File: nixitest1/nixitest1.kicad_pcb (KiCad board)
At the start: 2 copper layers, 22 x 38.2 mm, 34 parts, among them J1 MSYS, Q1 60V 3A, Q10 HVN, Q11 HVN, Q12 HVN, Q13 HVN, Q2 HVN, Q3 HVN, Q4 HVN, Q5 HVN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

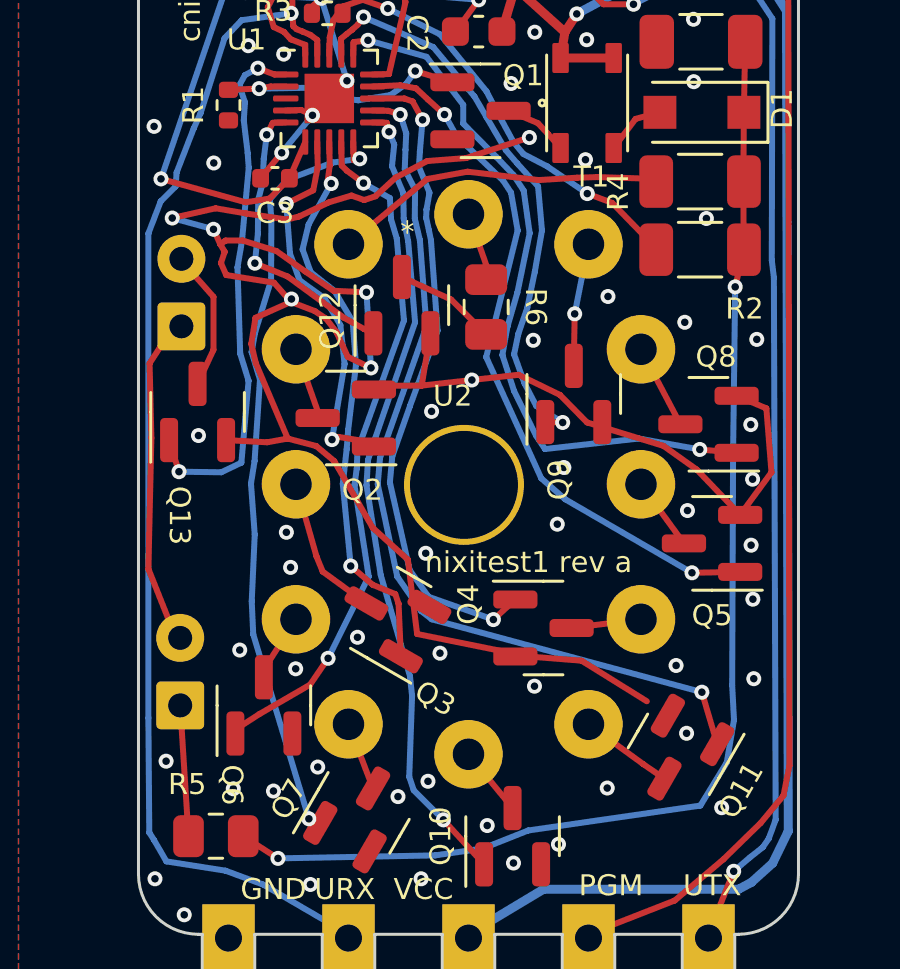
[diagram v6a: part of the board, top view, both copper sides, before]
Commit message: Update footprints to shrink holes for standoffs.
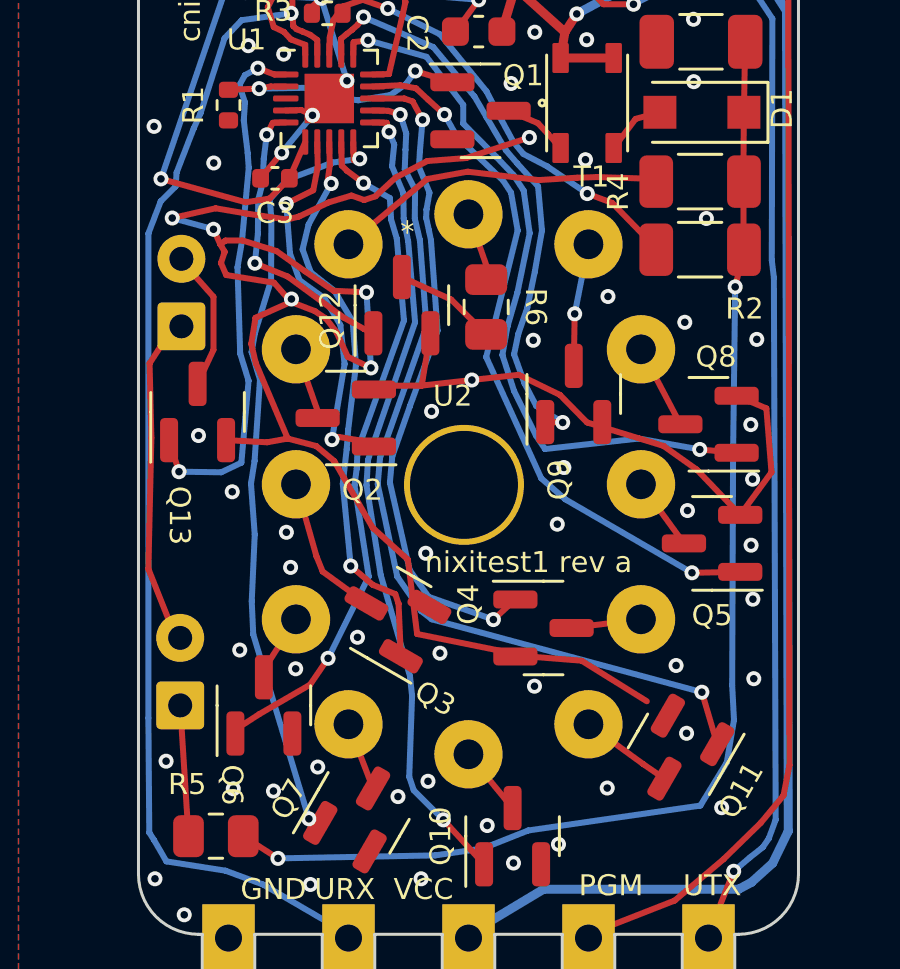
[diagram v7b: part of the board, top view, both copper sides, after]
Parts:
- R5, R6: value 68kΩ 125mW -> 82kΩ 125mW
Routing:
- net GND: vias 79 -> 80
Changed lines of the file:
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@@
     (descr "Resistor SMD 0805 (2012 Metric), square (rectangular) end terminal, IPC_7351 nominal, (Body size source: IPC-SM-782 page 72, https://www.pcb-3d.com/wordpress/wp-content/uploads/ipc-sm-782a_amendment_1_and_2.pdf), generated with kicad-footprint-generator")
     (tags "resistor")
-    (property "LCSC" "C114548")
+    (property "LCSC" "C136904")
     (property "Sheetfile" "nixitest1.kicad_sch")
     (property "Sheetname" "")
@@
       (effects (font (size 0.7 0.7) (thickness 0.1)))
     )
-    (fp_text value "68kΩ 125mW" (at 0 1.65 -90 unlocked) (layer "F.Fab")
+    (fp_text value "82kΩ 125mW" (at 0 1.65 -90 unlocked) (layer "F.Fab")
       (effects (font (size 1 1) (thickness 0.15)))
     )
@@
   (footprint "IN12-NIXIE:IN12-NIXIE" (layer "F.Cu")
     (at 90 80)
-    (property "LCSC" "")
+    (property "LCSC" "~")
     (property "Sheetfile" "nixitest1.kicad_sch")
     (property "Sheetname" "")
@@
     )
     (pad "" smd oval (at 0 0) (size 21 31) (property pad_prop_fiducial_loc) (layers "Dwgs.User"))
-    (pad "" np_thru_hole circle (at -0.15 0.02) (size 4 4) (drill 3.6) (layers F&B.Cu "F.Mask"))
-    (pad "1" thru_hole circle (at -4 -8) (size 2.286 2.286) (drill 1.05) (layers *.Cu *.Mask)
+    (pad "" np_thru_hole circle (at -0.15 0.02) (size 4 4) (drill 3.6) (layers F&B.Cu *.Mask))
+    (pad "1" thru_hole circle (at -4 -8) (size 2.28 2.28) (drill 0.99) (layers *.Cu *.Mask)
       (net 30 "ANODE") (pinfunction "A") (pintype "input"))
-    (pad "2" thru_hole circle (at -5.75 -4.5) (size 2.286 2.286) (drill 1.05) (layers *.Cu *.Mask)
+    (pad "2" thru_hole circle (at -5.75 -4.5) (size 2.28 2.28) (drill 0.99) (layers *.Cu *.Mask)
       (net 6 "CATH0") (pinfunction "K0") (pintype "input"))
-    (pad "3" thru_hole circle (at -5.75 0) (size 2.286 2.286) (drill 1.05) (layers *.Cu *.Mask)
+    (pad "3" thru_hole circle (at -5.75 0 180) (size 2.28 2.28) (drill 0.99) (layers *.Cu *.Mask)
       (net 8 "CATH1") (pinfunction "K9") (pintype "input"))
-    (pad "4" thru_hole circle (at -5.75 4.5) (size 2.286 2.286) (drill 1.05) (layers *.Cu *.Mask)
+    (pad "3" thru_hole circle (at -5.75 0 180) (size 2.28 2.28) (drill 0.99) (layers *.Cu *.Mask)
+      (net 8 "CATH1") (pinfunction "K9") (pintype "input"))
+    (pad "4" thru_hole circle (at -5.75 4.5) (size 2.28 2.28) (drill 0.99) (layers *.Cu *.Mask)
       (net 14 "CATH2") (pinfunction "K8") (pintype "input"))
-    (pad "5" thru_hole circle (at -4 8) (size 2.286 2.286) (drill 1.05) (layers *.Cu *.Mask)
+    (pad "5" thru_hole circle (at -4 8) (size 2.28 2.28) (drill 0.99) (layers *.Cu *.Mask)
       (net 16 "CATH3") (pinfunction "K7") (pintype "input"))
-    (pad "6" thru_hole circle (at 0 9) (size 2.286 2.286) (drill 1.05) (layers *.Cu *.Mask)
+    (pad "6" thru_hole circle (at 0 9) (size 2.28 2.28) (drill 0.99) (layers *.Cu *.Mask)
       (net 22 "CATH4") (pinfunction "K6") (pintype "input"))
-    (pad "7" thru_hole circle (at 4 8) (size 2.286 2.286) (drill 1.05) (layers *.Cu *.Mask)
+    (pad "7" thru_hole circle (at 4 8) (size 2.28 2.28) (drill 0.99) (layers *.Cu *.Mask)
       (net 24 "CATH5") (pinfunction "K5") (pintype "input"))
-    (pad "8" thru_hole circle (at 5.75 4.5) (size 2.286 2.286) (drill 1.05) (layers *.Cu *.Mask)
+    (pad "8" thru_hole circle (at 5.75 4.5) (size 2.28 2.28) (drill 0.99) (layers *.Cu *.Mask)
       (net 10 "CATH6") (pinfunction "K4") (pintype "input"))
-    (pad "9" thru_hole circle (at 5.75 0) (size 2.286 2.286) (drill 1.05) (layers *.Cu *.Mask)
+    (pad "9" thru_hole circle (at 5.75 0) (size 2.28 2.28) (drill 0.99) (layers *.Cu *.Mask)
       (net 12 "CATH7") (pinfunction "K3") (pintype "input"))
-    (pad "10" thru_hole circle (at 5.75 -4.5) (size 2.286 2.286) (drill 1.05) (layers *.Cu *.Mask)
+    (pad "10" thru_hole circle (at 5.75 -4.5) (size 2.28 2.28) (drill 0.99) (layers *.Cu *.Mask)
       (net 18 "CATH8") (pinfunction "K2") (pintype "input"))
-    (pad "11" thru_hole circle (at 4 -8) (size 2.286 2.286) (drill 1.05) (layers *.Cu *.Mask)
+    (pad "11" thru_hole circle (at 4 -8) (size 2.28 2.28) (drill 0.99) (layers *.Cu *.Mask)
       (net 20 "CATH9") (pinfunction "K1") (pintype "input"))
-    (pad "12" thru_hole circle (at 0 -9) (size 2.286 2.286) (drill 1.05) (layers *.Cu *.Mask)
+    (pad "12" thru_hole circle (at 0 -9) (size 2.28 2.28) (drill 0.99) (layers *.Cu *.Mask)
       (net 26 "CATHDOT") (pinfunction "Kd") (pintype "input"))
   )
@@
     (descr "Resistor SMD 0805 (2012 Metric), square (rectangular) end terminal, IPC_7351 nominal, (Body size source: IPC-SM-782 page 72, https://www.pcb-3d.com/wordpress/wp-content/uploads/ipc-sm-782a_amendment_1_and_2.pdf), generated with kicad-footprint-generator")
     (tags "resistor")
-    (property "LCSC" "C114548")
+    (property "LCSC" "C136904")
     (property "Sheetfile" "nixitest1.kicad_sch")
     (property "Sheetname" "")
@@
       (effects (font (size 0.7 0.7) (thickness 0.1)))
     )
-    (fp_text value "68kΩ 125mW" (at 0 1.65 unlocked) (layer "F.Fab")
+    (fp_text value "82kΩ 125mW" (at 0 1.65 unlocked) (layer "F.Fab")
       (effects (font (size 1 1) (thickness 0.15)))
     )
@@
   (via (at 92.96 81.33) (size 0.5) (drill 0.25) (layers "F.Cu" "B.Cu") (free) (net 1))
   (via (at 97.5 64.5) (size 0.5) (drill 0.25) (layers "F.Cu" "B.Cu") (free) (net 1))
+  (via (at 82.125 80.25) (size 0.5) (drill 0.25) (layers "F.Cu" "B.Cu") (free) (net 1))
   (via (at 79.61 59.7) (size 0.5) (drill 0.25) (layers "F.Cu" "B.Cu") (free) (net 1))
   (via (at 99.51 86.48) (size 0.5) (drill 0.25) (layers "F.Cu" "B.Cu") (free) (net 1))

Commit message: Update to rev B.
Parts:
- C1: footprint Capacitor_SMD:C_1206_3216Metric -> Capacitor_SMD:C_1210_3225Metric
- C3: value 100n -> 220nF
- moved D1 0.38 mm to (97.8, 68.0)
- moved R2 0.38 mm to (97.7, 72.6)
- moved R4 0.38 mm to (97.7, 70.3)
- moved T1 0.09 mm to (93.9, 67.3)
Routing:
- net GND: track 131.3 -> 144.9 mm, vias 80 -> 83
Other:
- board text added: "nixitest1 rev b"
- board text removed: "nixitest1 rev a"
